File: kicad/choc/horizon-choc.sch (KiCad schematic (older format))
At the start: 117 parts, among them SW1 SW_Push, SW10 SW_Push, SW11 SW_Push, SW12 SW_Push, SW13 SW_Push, SW14 SW_Push, SW15 SW_Push, SW16 SW_Push, SW17 SW_Push, SW18 SW_Push, SW19 SW_Push, SW2 SW_Push, SW20 SW_Push, SW21 SW_Push, SW22 SW_Push, SW23 SW_Push, SW24 SW_Push, SW25 SW_Push, SW26 SW_Push, SW27 SW_Push, SW28 SW_Push, SW29 SW_Push, SW3 SW_Push, SW30 SW_Push, SW31 SW_Push, SW32 SW_Push, SW33 SW_Push, SW34 SW_Push, SW35 SW_Push, SW36 SW_Push, SW37 SW_Push, SW38 SW_Push, SW39 SW_Push, SW4 SW_Push, SW40 SW_Push, SW41 SW_Push, SW42 SW_Push, SW43 SW_Push, SW44 SW_Push, SW45 SW_Push, SW46 SW_Push, SW47 SW_Push, SW48 SW_Push, SW49 SW_Push, SW5 SW_Push, SW50 SW_Push, SW51 SW_Push, SW52 SW_Push, SW6 SW_Push, SW7 SW_Push, SW8 SW_Push, SW9 SW_Push, U1 PRO-MICRO

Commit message: Clean up plate cuts, update MX board with battery removed
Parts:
- removed SS1: POWER, horizon-footprints:SS12D00, symbol horizon-components:SW_SPDT
- removed TB1: BATTERY, horizon-footprints:KF350-2P, symbol horizon-components:Conn_01x02
- SW1, SW10, SW11, SW12, SW13, SW14, SW15, SW16, SW17, SW18, SW19, SW2, SW20, SW21, SW22, SW23, SW24, SW25, SW26, SW27, SW28, SW29, SW3, SW30, SW31, SW32, SW33, SW34, SW35, SW36, SW37, SW38, SW39, SW4, SW40, SW41, SW42, SW43, SW44, SW45, SW46, SW47, SW48, SW49, SW5, SW50, SW51, SW52, SW6, SW7, SW8, SW9: footprint horizon-footprints:SW_MX -> horizon-footprints:SW_Choc
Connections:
- net labels removed: +BATT, RAW
- wire segments 175 -> 169
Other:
- moved on the sheet: BTN1

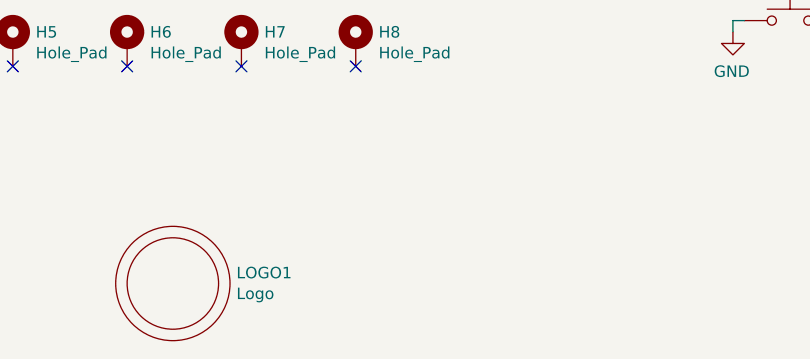
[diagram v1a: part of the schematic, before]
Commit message: Preserve logos on plate PCBs
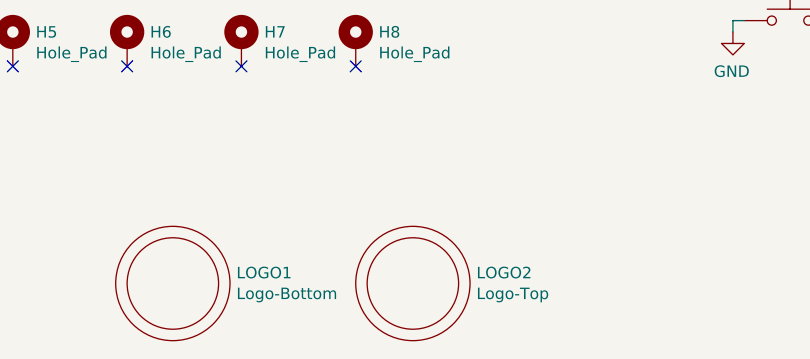
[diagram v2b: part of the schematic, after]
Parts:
- added LOGO2: Logo-Top, horizon-footprints:Logo_Horizon_H, symbol horizon-components:Logo
- LOGO1: value Logo -> Logo-Bottom
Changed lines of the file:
@@
 EESchema Schematic File Version 4
-LIBS:horizon-choc-cache
 EELAYER 30 0
 EELAYER END
@@
 P 2400 6400
 F 0 "LOGO1" H 2678 6446 50  0000 L CNN
-F 1 "Logo" H 2678 6355 50  0000 L CNN
+F 1 "Logo-Bottom" H 2678 6355 50  0000 L CNN
 F 2 "horizon-footprints:Logo_Horizon_Small" H 2400 6350 50  0001 C CNN
 F 3 "" H 2400 6350 50  0001 C CNN
@@
 COL1
 NoConn ~ 7700 4900
+$Comp
+L horizon-components:Logo LOGO2
+U 1 1 61512730
+P 3450 6400
+F 0 "LOGO2" H 3728 6446 50  0000 L CNN
+F 1 "Logo-Top" H 3728 6355 50  0000 L CNN
+F 2 "horizon-footprints:Logo_Horizon_H" H 3450 6350 50  0001 C CNN
+F 3 "" H 3450 6350 50  0001 C CNN
+	1    3450 6400
+	1    0    0    -1
+$EndComp
 $EndSCHEMATC
